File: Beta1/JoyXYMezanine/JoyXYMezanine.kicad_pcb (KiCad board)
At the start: 2 copper layers, 26.5 x 30.9 mm, 17 parts

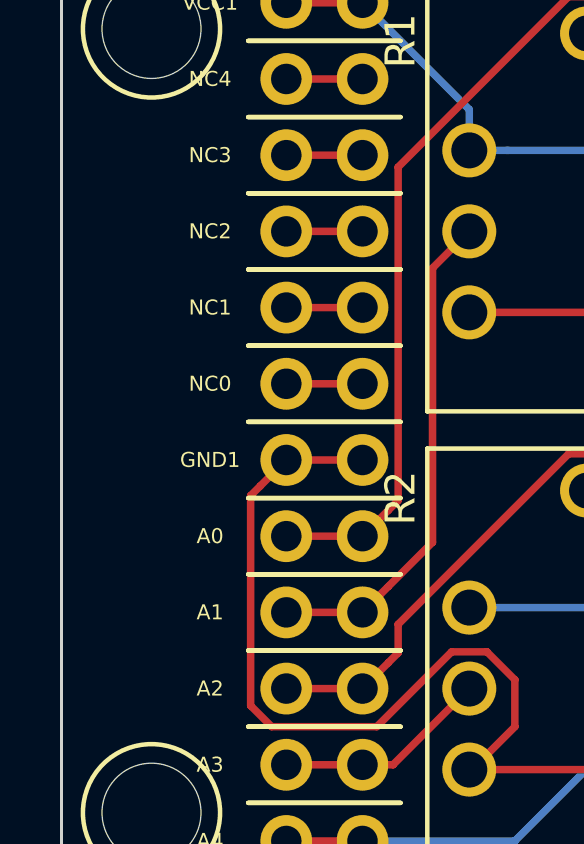
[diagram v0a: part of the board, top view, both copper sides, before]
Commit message: Added board date / info.
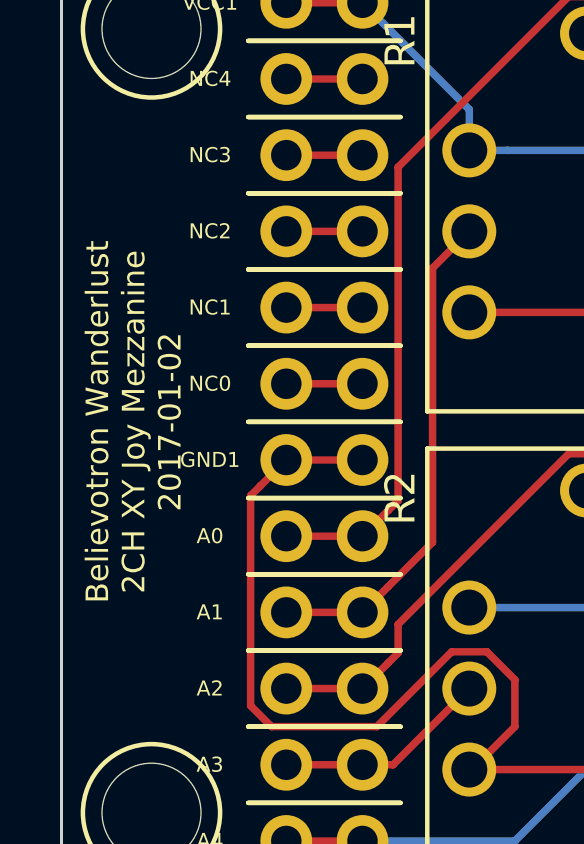
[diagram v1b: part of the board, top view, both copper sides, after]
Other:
- board text added: "Believotron Wanderlust 2CH XY Joy Mezzanine 2017-01-02"
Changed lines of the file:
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@@
     (area -0.050001 -31.537501 26.550001 -0.587499)
     (thickness 1.6)
-    (drawings 14)
+    (drawings 15)
     (tracks 68)
     (zones 0)
@@
       (net 12 VCC))
   )
+  (gr_text "Believotron Wanderlust \n2CH XY Joy Mezzanine\n2017-01-02" (at 2.413 -16.0274 90) (layer F.SilkS)
+    (effects (font (size 0.75 0.75) (thickness 0.1875)))
+  )
   (gr_line (start 185.76 -32.1253) (end 25.76 -32.1253) (layer Dwgs.User) (width 0.2))
